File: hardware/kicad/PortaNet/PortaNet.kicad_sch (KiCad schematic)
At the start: 0 parts

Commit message: eod commit
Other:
- added sheet misc1 (misc1.kicad_sch)
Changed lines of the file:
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@@
+    )
+  )
+  (sheet (at 39.37 47.625) (size 34.29 10.16) (fields_autoplaced)
+    (stroke (width 0.1524) (type solid) (color 0 0 0 0))
+    (fill (color 0 0 0 0.0000))
+    (property "Sheet name" "misc1" (id 0) (at 39.37 46.9134 0)
+      (effects (font (size 1.27 1.27)) (justify left bottom))
+    )
+    (property "Sheet file" "misc1.kicad_sch" (id 1) (at 39.37 58.3696 0)
+      (effects (font (size 1.27 1.27)) (justify left top))
     )
   )
@@
     (path "/" (page "1"))
     (path "/1e5d0253-acc2-4f0d-86a2-9343225c71a7" (page "2"))
+    (path "/5873cb1d-2980-4d04-84de-c428523b74e7" (page "3"))
   )
   (symbol_instances
+    (path "/1e5d0253-acc2-4f0d-86a2-9343225c71a7/b956589f-9db6-424e-b8ba-0903b7f520ec"
+      (reference "#PWR0101") (unit 1) (value "GND") (footprint "")
+    )
     (path "/1e5d0253-acc2-4f0d-86a2-9343225c71a7/65235f14-32b1-40c3-9f6b-21412c001e81"
-      (reference "#PWR?") (unit 1) (value "GND") (footprint "")
+      (reference "#PWR0102") (unit 1) (value "GND") (footprint "")
+    )
+    (path "/1e5d0253-acc2-4f0d-86a2-9343225c71a7/3045ca6f-6303-47ce-9efc-bca23d998961"
+      (reference "#PWR0103") (unit 1) (value "GND") (footprint "")
+    )
+    (path "/1e5d0253-acc2-4f0d-86a2-9343225c71a7/fff88ac9-0aea-4d3f-8e5a-1f9d4618c83b"
+      (reference "#PWR0104") (unit 1) (value "GND") (footprint "")
+    )
+    (path "/1e5d0253-acc2-4f0d-86a2-9343225c71a7/7211f8d4-62b0-4c2b-a370-dcb9b31c2fcd"
+      (reference "#PWR0105") (unit 1) (value "GND") (footprint "")
+    )
+    (path "/5873cb1d-2980-4d04-84de-c428523b74e7/78978477-abfe-400a-be9d-d34caba8ef08"
+      (reference "#PWR0106") (unit 1) (value "GND") (footprint "")
+    )
+    (path "/5873cb1d-2980-4d04-84de-c428523b74e7/4fc5c441-8476-4709-8595-a6075bf2d580"
+      (reference "#PWR0107") (unit 1) (value "GND") (footprint "")
+    )
+    (path "/1e5d0253-acc2-4f0d-86a2-9343225c71a7/0f71d965-26d5-42e8-b8da-c7f912ad95c8"
+      (reference "C?") (unit 1) (value "0.1uF") (footprint "Capacitor_SMD:C_0603_1608Metric")
+    )
+    (path "/1e5d0253-acc2-4f0d-86a2-9343225c71a7/3295f611-6ce3-4ca8-b291-32848720480c"
+      (reference "C?") (unit 1) (value "0.1uF") (footprint "Capacitor_SMD:C_0603_1608Metric")
+    )
+    (path "/1e5d0253-acc2-4f0d-86a2-9343225c71a7/7416e59d-d321-429d-bdc1-ea2653465baf"
+      (reference "C?") (unit 1) (value "10uF") (footprint "Capacitor_SMD:C_0603_1608Metric")
+    )
+    (path "/5873cb1d-2980-4d04-84de-c428523b74e7/807215d9-1c49-4932-ac74-264d93dcfa83"
+      (reference "C?") (unit 1) (value "10uF") (footprint "Capacitor_SMD:C_0603_1608Metric")
+    )
+    (path "/1e5d0253-acc2-4f0d-86a2-9343225c71a7/89428f88-23f1-4263-88c8-56bdcc2e25c3"
+      (reference "C?") (unit 1) (value "0.1uF") (footprint "Capacitor_SMD:C_0603_1608Metric")
+    )
+    (path "/1e5d0253-acc2-4f0d-86a2-9343225c71a7/b497ac16-865d-4d08-a87b-14900ca1427d"
+      (reference "C?") (unit 1) (value "10uF") (footprint "Capacitor_SMD:C_0603_1608Metric")
+    )
+    (path "/1e5d0253-acc2-4f0d-86a2-9343225c71a7/b58b5d5e-bfc9-40cb-897c-7cabd57af31d"
+      (reference "C?") (unit 1) (value "10uF") (footprint "Capacitor_SMD:C_0603_1608Metric")
+    )
+    (path "/1e5d0253-acc2-4f0d-86a2-9343225c71a7/cfad5c7d-b13d-4d54-9917-ceea16583277"
+      (reference "C?") (unit 1) (value "0.1uF") (footprint "Capacitor_SMD:C_0603_1608Metric")
+    )
+    (path "/5873cb1d-2980-4d04-84de-c428523b74e7/f18d7b7b-e771-4659-b7d2-4766cb7b211d"
+      (reference "C?") (unit 1) (value ".1uF") (footprint "Capacitor_SMD:C_0603_1608Metric")
+    )
+    (path "/1e5d0253-acc2-4f0d-86a2-9343225c71a7/f65d786d-fc9d-482b-bb95-2977674749d8"
+      (reference "C?") (unit 1) (value "10uF") (footprint "Capacitor_SMD:C_0603_1608Metric")
     )
     (path "/1e5d0253-acc2-4f0d-86a2-9343225c71a7/b97ff70e-3997-4b11-bc73-1102f98616a3"
       (reference "U?") (unit 1) (value "ESP32-C3") (footprint "Package_DFN_QFN:QFN-32-1EP_5x5mm_P0.5mm_EP3.7x3.7mm_ThermalVias")
     )
+    (path "/5873cb1d-2980-4d04-84de-c428523b74e7/f607fb80-96f7-4a77-bfa8-4b29c1d49858"
+      (reference "U?") (unit 1) (value "AP2114HA-3.3TRG1") (footprint "Package_TO_SOT_SMD:SOT-223-3_TabPin2")
+    )
   )

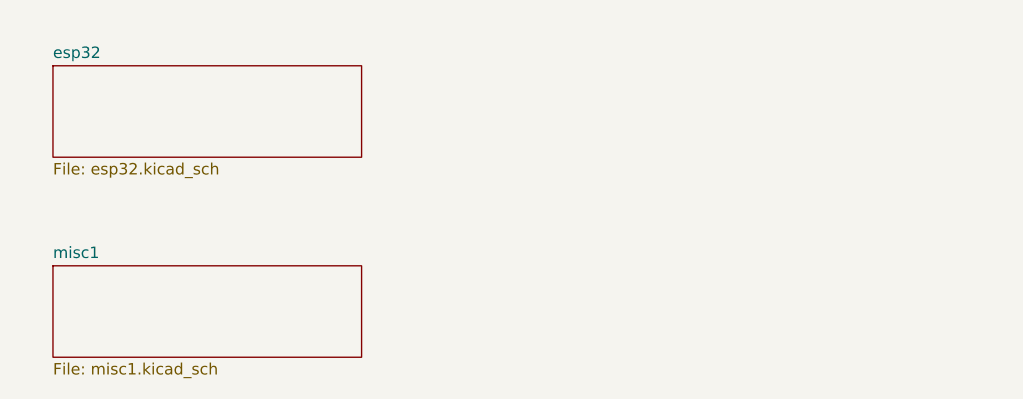
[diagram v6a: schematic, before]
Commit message: add bom
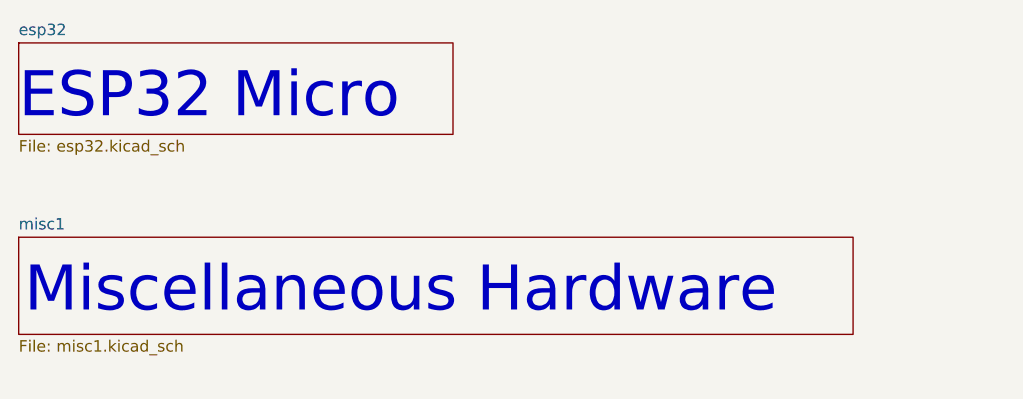
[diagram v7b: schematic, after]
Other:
- note added: "ESP32 Micro"
- note added: "Miscellaneous Hardware"
- company: (none) -> JCM
- title: (none) -> PortaNet
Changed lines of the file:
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@@
 (kicad_sch (version 20211123) (generator eeschema)
   (paper "A4")
-  (sheet (at 39.37 25.4) (size 34.29 10.16) (fields_autoplaced)
+  (title_block
+    (title "PortaNet")
+    (date "2022-03-12")
+    (rev "1.0")
+    (company "JCM")
+  )
+  (text "Miscellaneous Hardware" (at 36.195 53.34 0)
+    (effects (font (size 5 5)) (justify left bottom))
+  )
+  (text "ESP32 Micro" (at 35.56 31.75 0)
+    (effects (font (size 5 5)) (justify left bottom))
+  )
+  (sheet (at 35.56 22.86) (size 48.26 10.16) (fields_autoplaced)
     (stroke (width 0.1524) (type solid) (color 0 0 0 0))
     (fill (color 0 0 0 0.0000))
-    (property "Sheet name" "esp32" (id 0) (at 39.37 24.6884 0)
+    (property "Sheet name" "esp32" (id 0) (at 35.56 22.1484 0)
       (effects (font (size 1.27 1.27)) (justify left bottom))
     )
-    (property "Sheet file" "esp32.kicad_sch" (id 1) (at 39.37 36.1446 0)
+    (property "Sheet file" "esp32.kicad_sch" (id 1) (at 35.56 33.6046 0)
       (effects (font (size 1.27 1.27)) (justify left top))
     )
   )
-  (sheet (at 39.37 47.625) (size 34.29 10.16) (fields_autoplaced)
+  (sheet (at 35.56 44.45) (size 92.71 10.795) (fields_autoplaced)
     (stroke (width 0.1524) (type solid) (color 0 0 0 0))
     (fill (color 0 0 0 0.0000))
-    (property "Sheet name" "misc1" (id 0) (at 39.37 46.9134 0)
+    (property "Sheet name" "misc1" (id 0) (at 35.56 43.7384 0)
       (effects (font (size 1.27 1.27)) (justify left bottom))
     )
-    (property "Sheet file" "misc1.kicad_sch" (id 1) (at 39.37 58.3696 0)
+    (property "Sheet file" "misc1.kicad_sch" (id 1) (at 35.56 55.8296 0)
       (effects (font (size 1.27 1.27)) (justify left top))
     )
